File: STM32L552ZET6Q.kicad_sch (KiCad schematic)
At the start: 34 parts, among them SW501 MCU_RST, U501 STM32L552ZET6Q, Y501 32.768kHz, 1.2pF, Y502 16MHz, 7pF

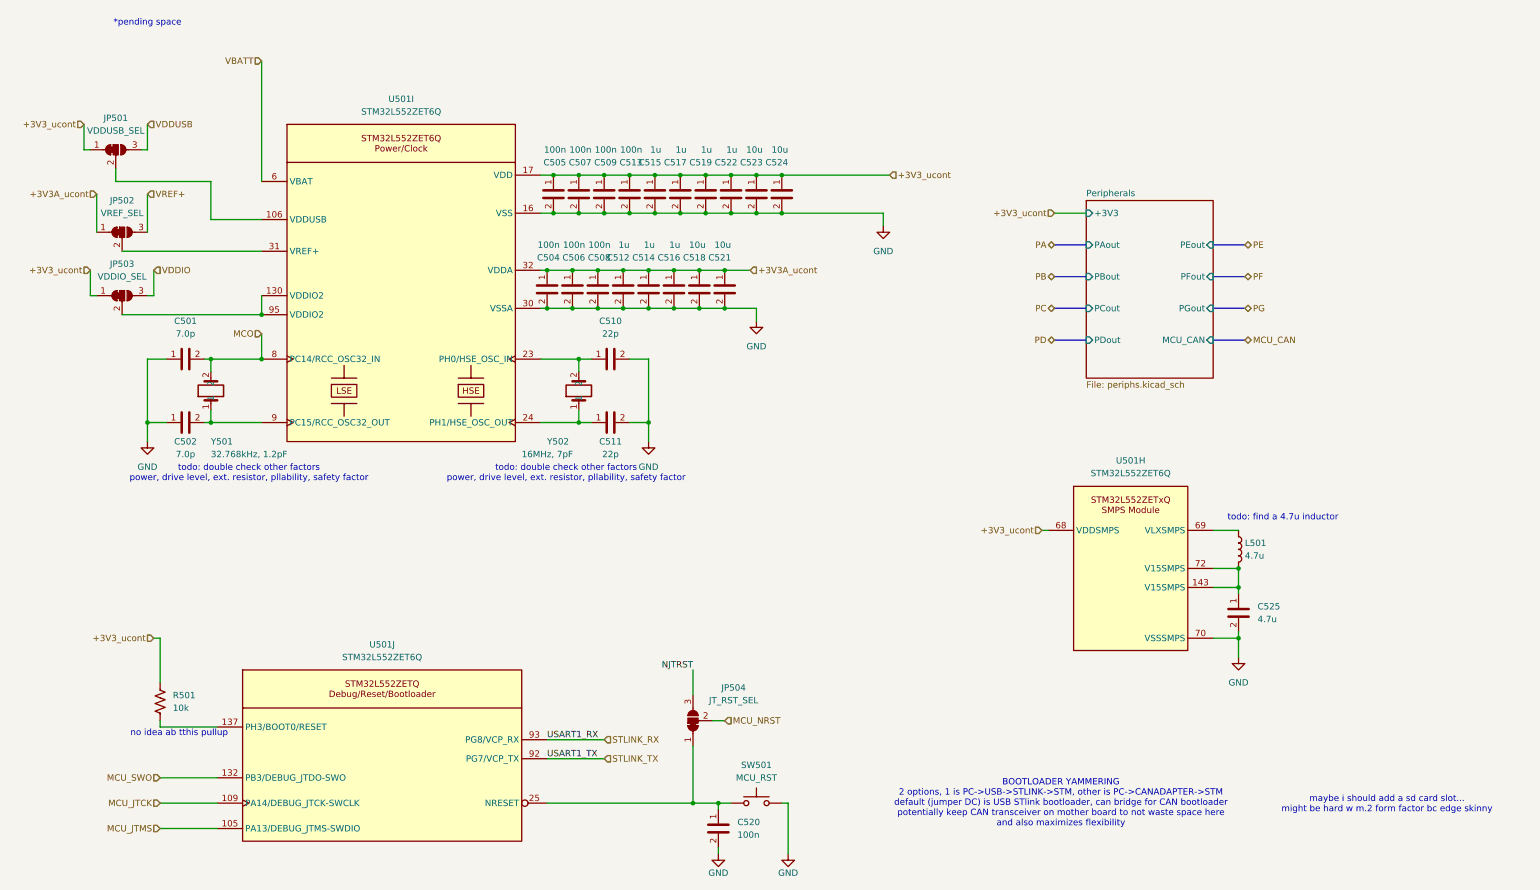
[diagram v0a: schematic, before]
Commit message: jk im stupid forgot to route the flash
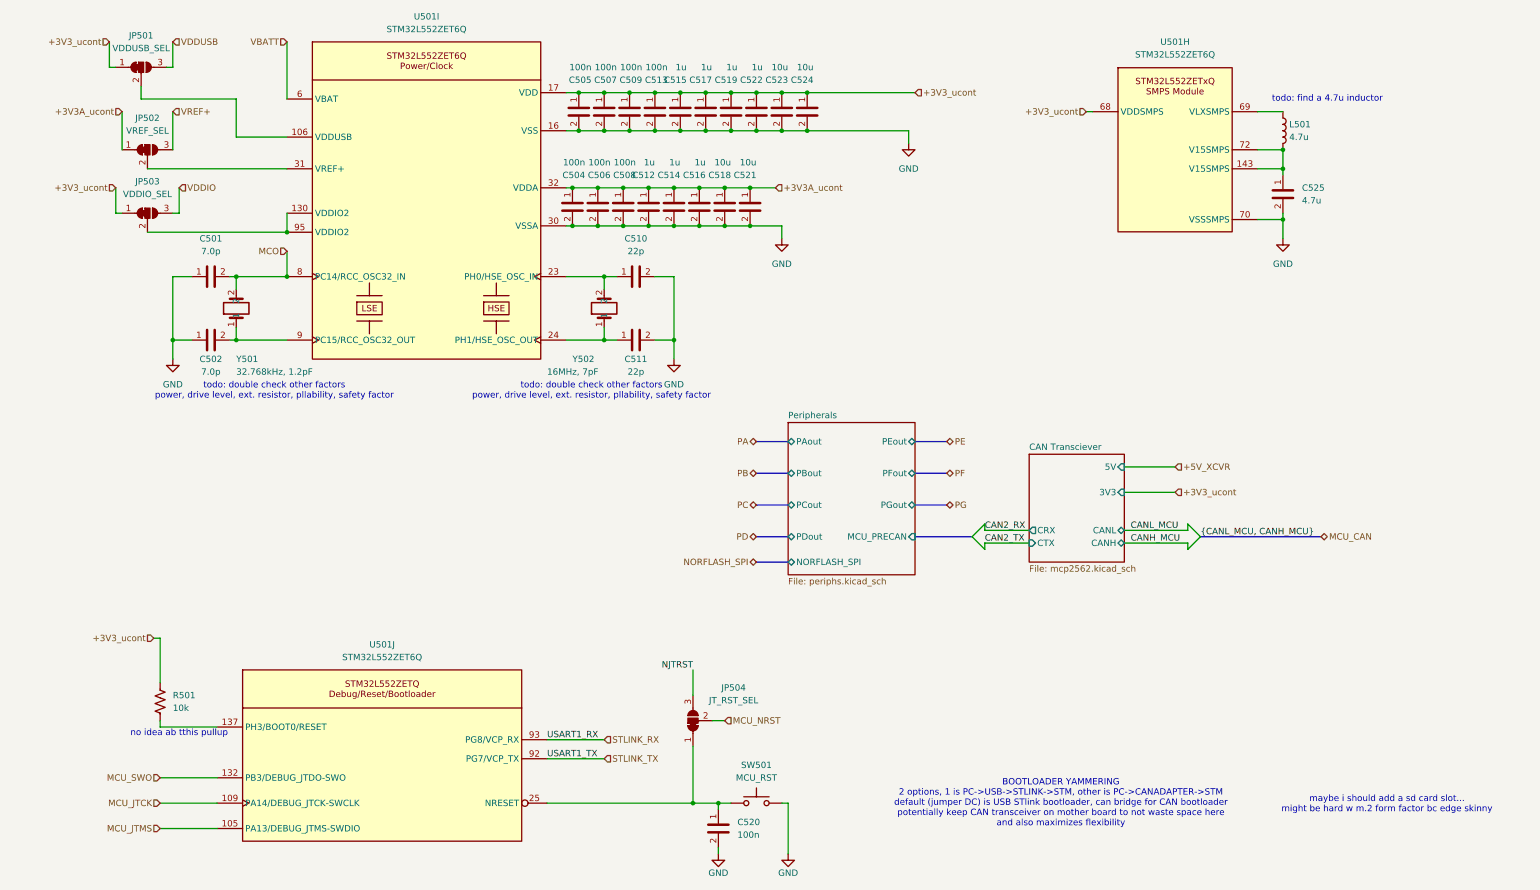
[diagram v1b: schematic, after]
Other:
- added sheet CAN Transciever (mcp2562.kicad_sch)
- sheet Peripherals ports: added MCU_PRECAN, NORFLASH_SPI; removed +3V3, MCU_CAN
- note removed: "*pending space"
- moved on the sheet: C501, C502, C504, C505, C506, C507, C508, C509, C510, C511, C512, C513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

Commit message: fixed like a bunch of things, power and new xcvr and lights and other goodies, also started layout
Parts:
- removed C512, C514, C515, C516, C517, C519, C522: 1u, Capacitor_SMD:C_0402_1005Metric_Pad0.74x0.62mm_HandSolder, symbol bfr_capacitors:CL05A105KA5NQNC
- removed C518, C521, C523, C524: 10u, Capacitor_SMD:C_0603_1608Metric_Pad1.08x0.95mm_HandSolder, symbol bfr_capacitors:CL10A106MA8NRNC
- removed L501: 4.7u, symbol Device:L
- added C511, C513, C514, C515, C516, C518, C519, C520, C521, C522, C523, C524, C525: 100n, Capacitor_SMD:C_0402_1005Metric_Pad0.74x0.62mm_HandSolder, symbol bfr_capacitors:CL05B104KB54PNC
- added L501: 4.7u, bfr_inductors:BWVS005050404R7M00, symbol bfr_inductors:BWVS005050404R7M00
- JP501, JP502, JP503, JP504: footprint (none) -> Jumper:SolderJumper-3_P1.3mm_Bridged2Bar12_Pad1.0x1.5mm_NumberLabels
- SW501: footprint (none) -> Button_Switch_SMD:SW_Push_1P1T-SH_NO_CK_KMR2xxG
- renumbered C504 to C503, C505 to C504, C506 to C505, C507 to C506, C508 to C507, C509 to C508, C510 to C509, C511 to C510, C513 to C512, C520 to C517, C525 to C526
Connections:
- net +3V3A_ucont: now also C511.1, C513.1, C515.1, C518.1, C520.1
- net GND: now also C511.2, C513.2, C514.2, C515.2, C516.2, C518.2, C519.2, C520.2, C521.2, C522.2, C523.2, C524.2, C525.2
- net VDD: now also C514.1, C516.1, C519.1, C521.1, C522.1, C523.1, C524.1, C525.1
- net at C526.1, U501.143 (V15SMPS), U501.72 (V15SMPS): now also L501.1
- net at U501.69 (VLXSMPS): now also L501.2
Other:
- sheet CAN Transciever ports: added none; removed 5V
- sheet Peripherals ports: added LED_ARR_DATA; removed none
- note added: "120mA max from datasheet pg 147"

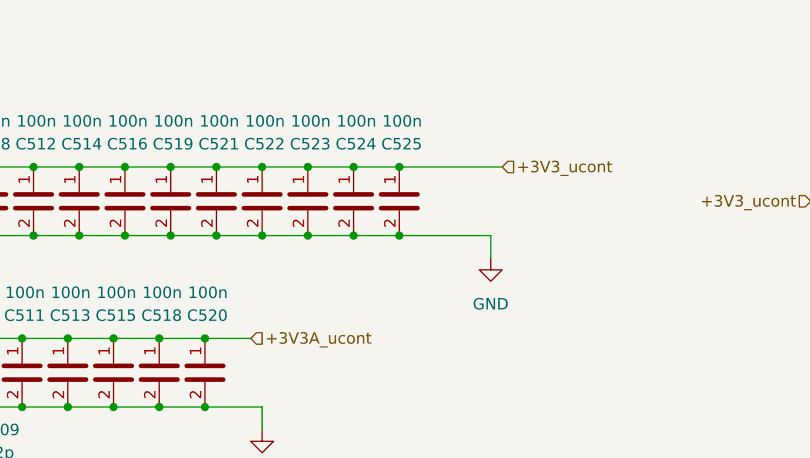
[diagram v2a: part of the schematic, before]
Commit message: quicksave on some R.S. T.S. (mostly layout changes, small pin changes for better routing)
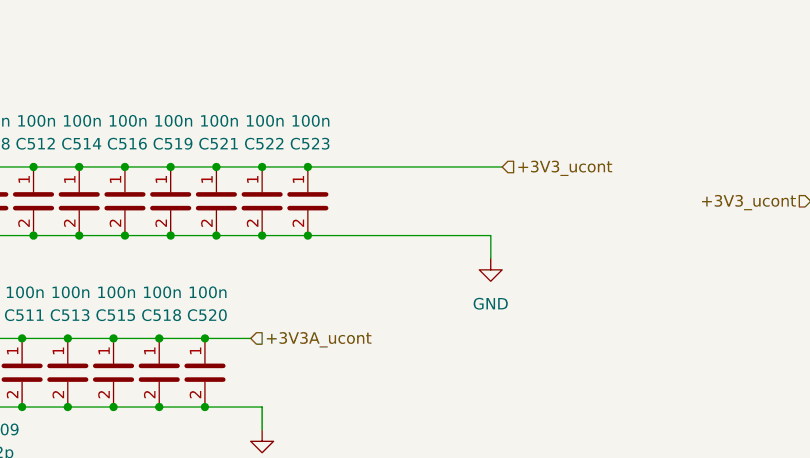
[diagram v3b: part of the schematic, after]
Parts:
- removed C524, C525: 100n, Capacitor_SMD:C_0402_1005Metric_Pad0.74x0.62mm_HandSolder, symbol bfr_capacitors:CL05B104KB54PNC

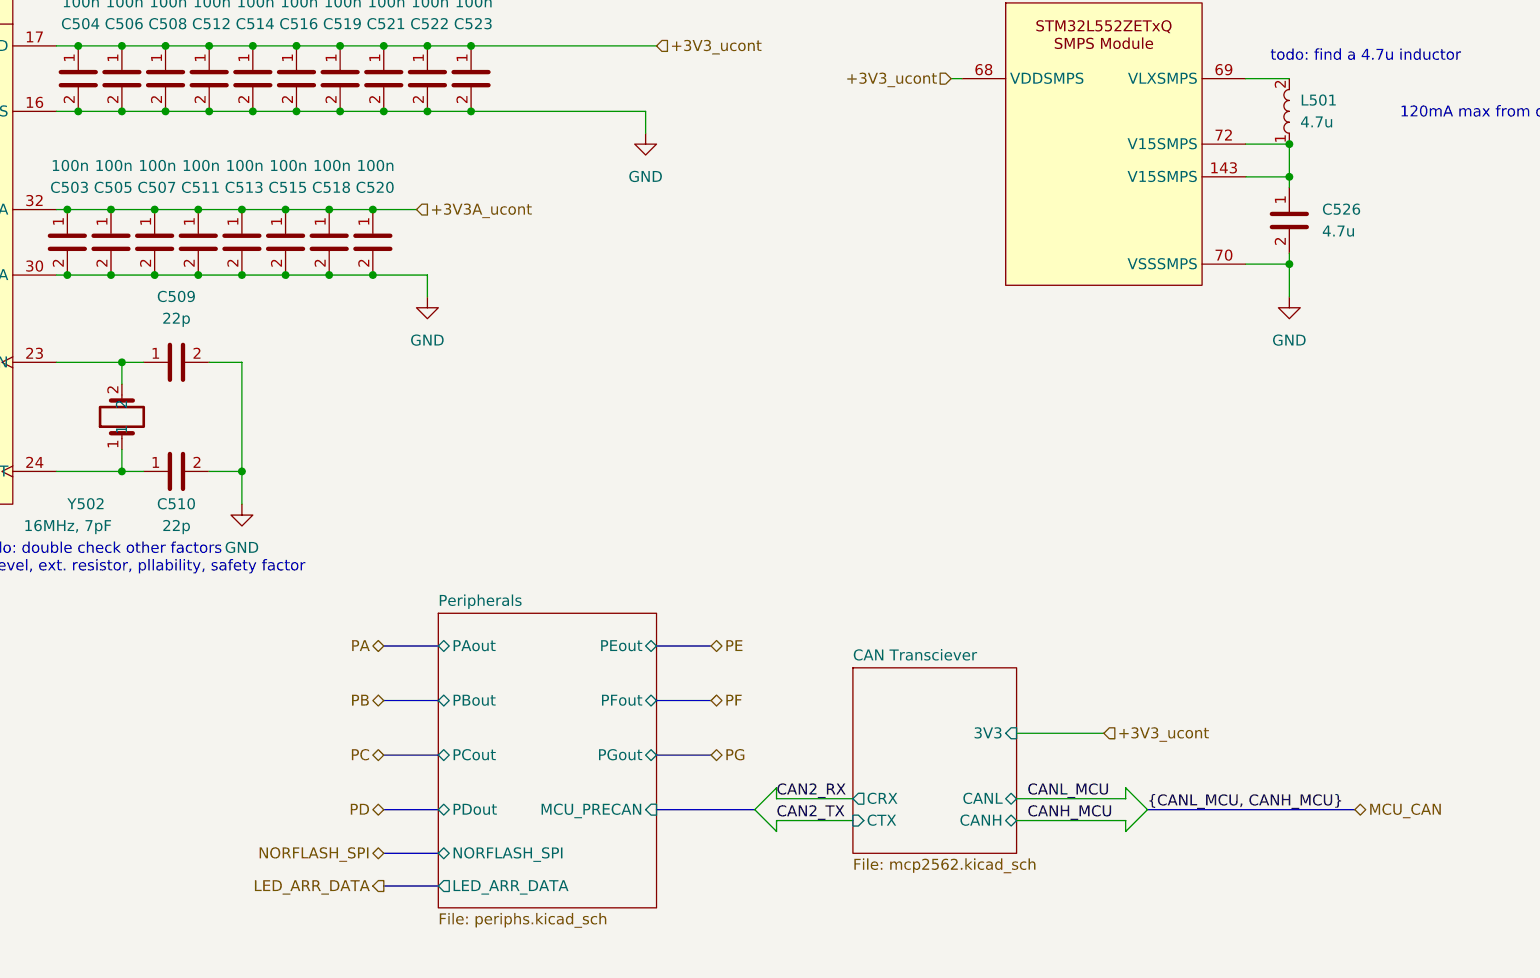
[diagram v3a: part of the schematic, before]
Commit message: laid out most of power, main xcvr, prob some other stuff
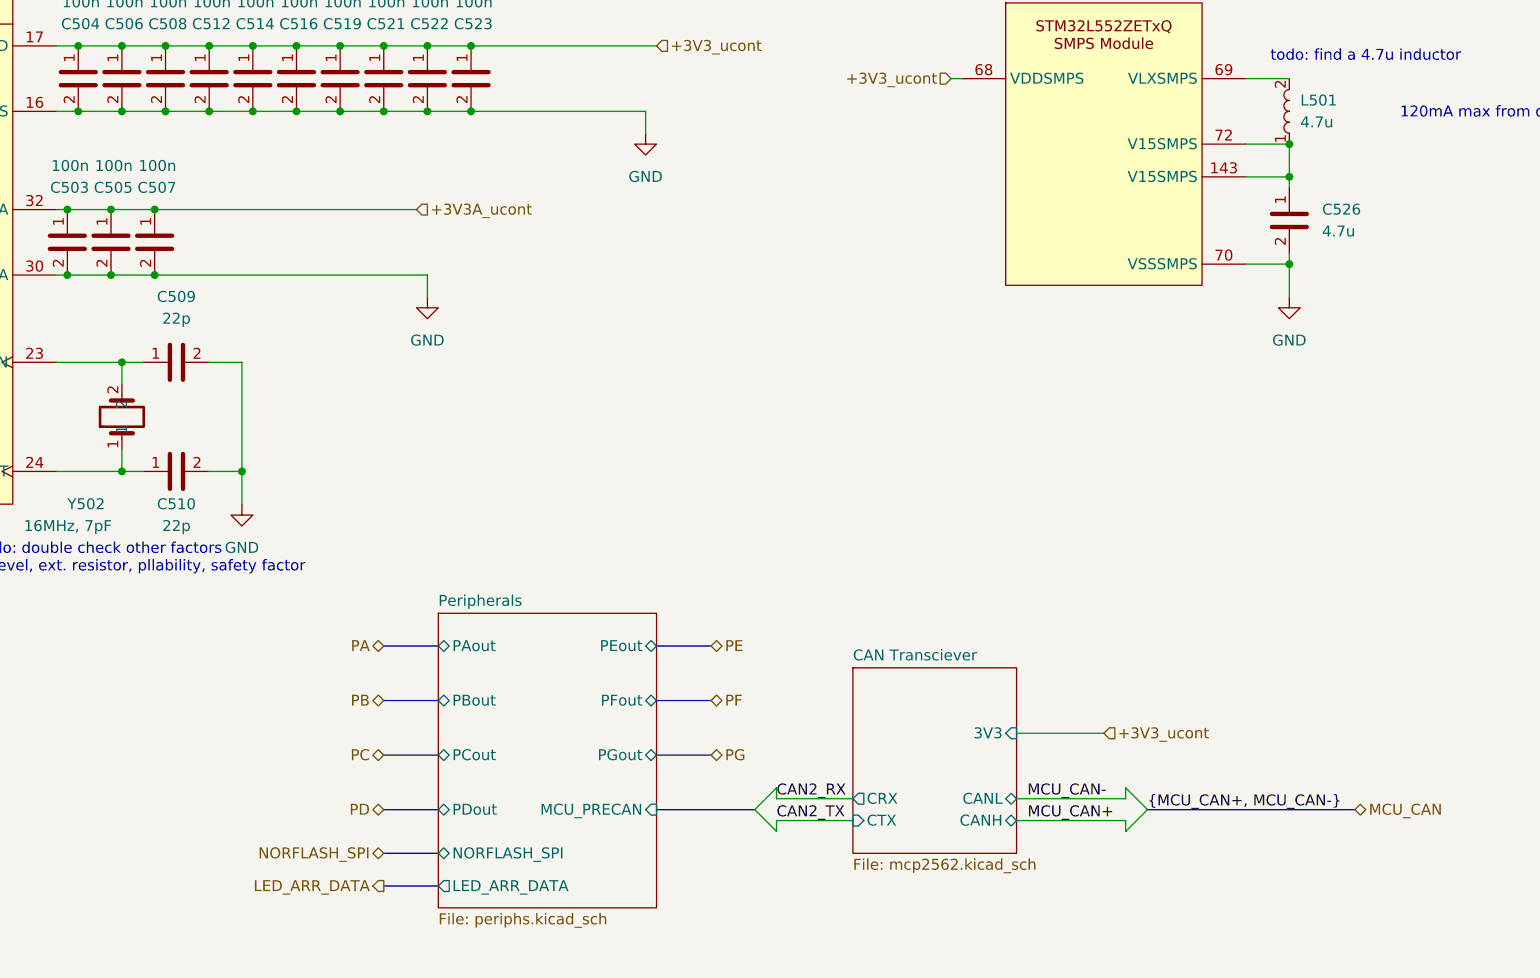
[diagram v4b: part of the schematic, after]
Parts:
- removed C511, C513, C515, C518, C520: 100n, Capacitor_SMD:C_0402_1005Metric_Pad0.74x0.62mm_HandSolder, symbol bfr_capacitors:CL05B104KB54PNC

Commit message: i fucken rerouted everything and redid the pinout like 3x, half routed GPIOs
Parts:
- removed C526: 4.7u, Capacitor_SMD:C_0603_1608Metric_Pad1.08x0.95mm_HandSolder, symbol bfr_capacitors:CL10A475KO8NNNC
- removed L501: 4.7u, bfr_inductors:BWVS005050404R7M00, symbol bfr_inductors:BWVS005050404R7M00
- removed Y502: 16MHz, 7pF, Crystal:Crystal_SMD_HC49-SD, symbol bfr_utilities:AS-16.000-18-SMD-TR
- added Y502: 16MHz, 7pF, bfr_crystals:ABM3-16.000MHZ-D2Y-T, symbol bfr_utilities:ABM3-16.000MHZ-D2Y-T
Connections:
- net GND: no longer U501.70 (VSSSMPS)
- net VDD: no longer U501.68 (VDDSMPS)
- net at U501.143 (V15SMPS): no longer U501.72 (V15SMPS)
- net at C510.1, U501.24 (PH1/HSE_OSC_OUT): now also Y502.2
- net at C509.1, U501.23 (PH0/HSE_OSC_IN): now also Y502.1
- no-connect marks 0 -> 5
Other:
- note removed: "120mA max from datasheet pg 147"
- note removed: "todo: find a 4.7u inductor"

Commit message: holy fucking stupid ass why did u put this upon urself
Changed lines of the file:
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@@
+		)
+	)
+	(label "{CAN2_TX,CAN2_RX}"
+		(at 191.77 120.65 0)
+		(effects
+			(font
+				(size 1.27 1.27)
+			)
+			(justify left bottom)
 		)
 	)

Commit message: fucking shit bro i like expanded the board by 1mm and it still has no room fuck this bitchass crystal
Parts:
- removed C512: 100n, Capacitor_SMD:C_0402_1005Metric_Pad0.74x0.62mm_HandSolder, symbol bfr_capacitors:CL05B104KB54PNC
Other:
- moved on the sheet: C514, C516, C519, C521, C522, C523
